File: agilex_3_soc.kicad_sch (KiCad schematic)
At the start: 5 parts, among them J1 Conn_01x14, J2 Conn_02x03_Odd_Even, J3 Conn_02x19_Odd_Even, J4 Conn_01x03, U1 IS43LQ32256A-062BLI

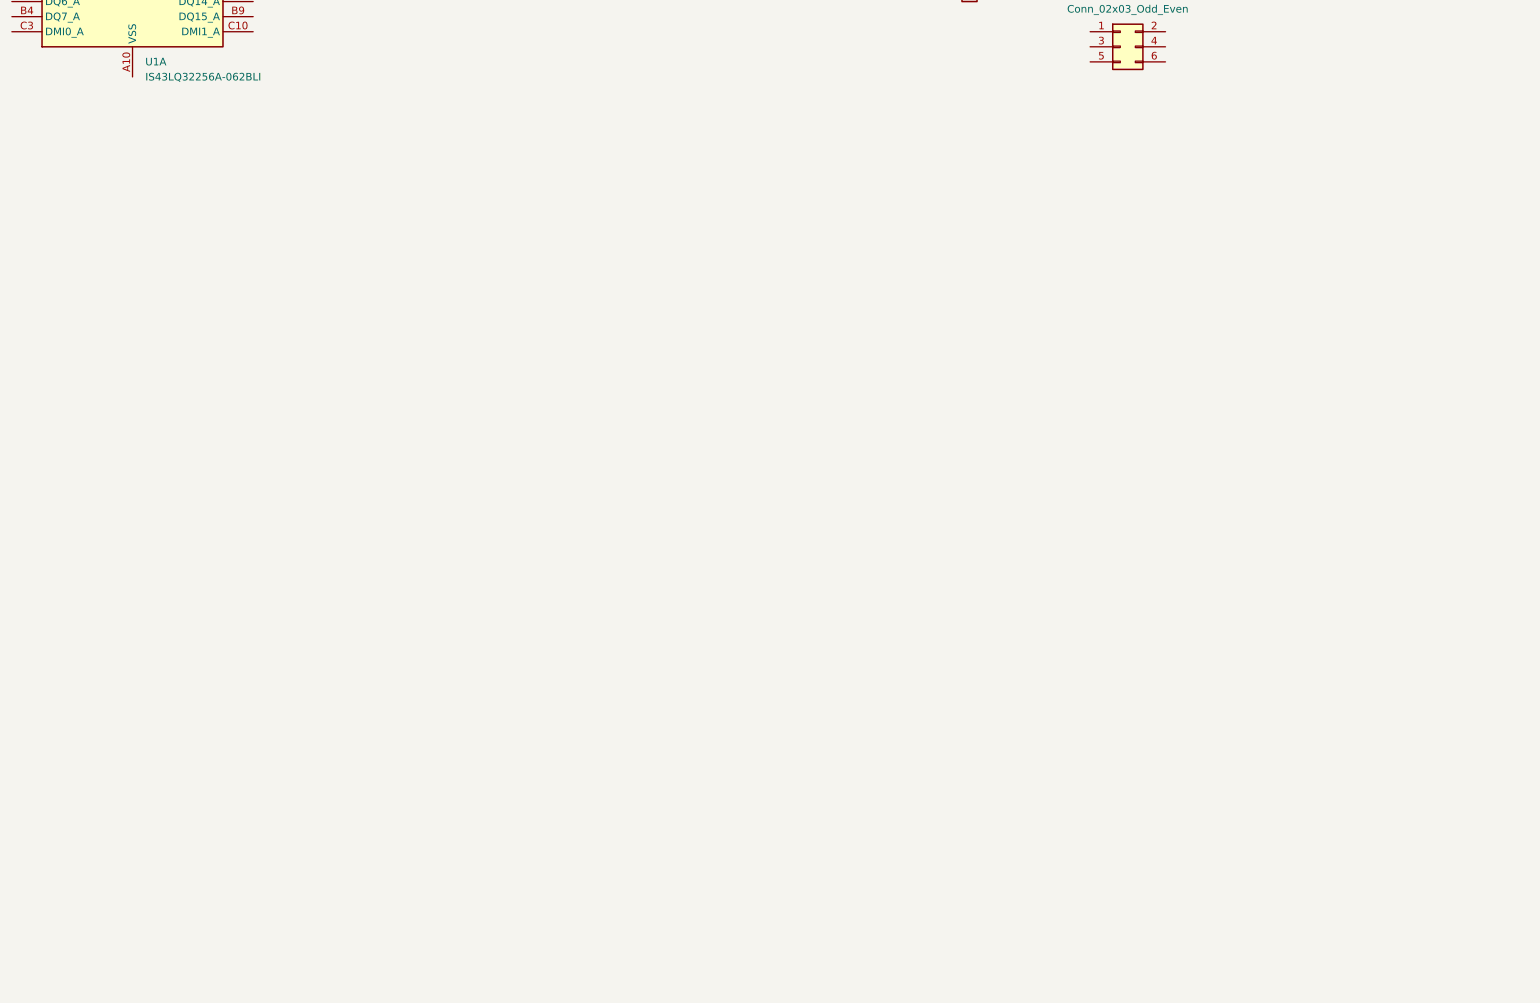
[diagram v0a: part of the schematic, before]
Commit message: sketch out more components from original design
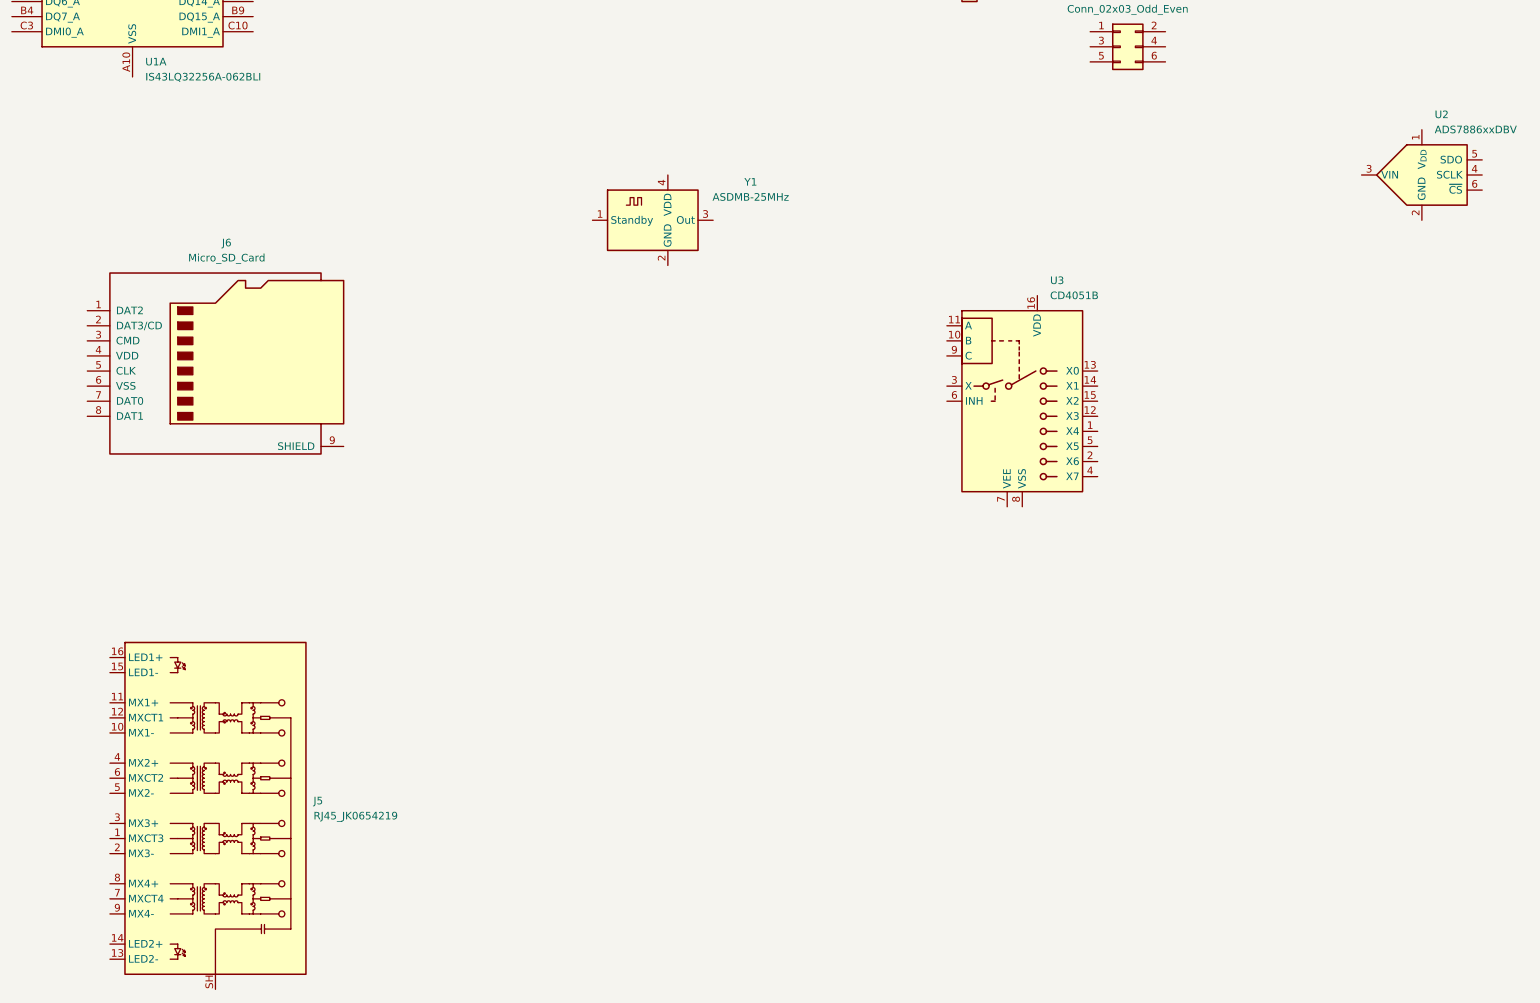
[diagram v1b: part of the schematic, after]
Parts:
- added J5: RJ45_JK0654219, Connector_RJ:RJ45_Pulse_JK0654219NL_Horizontal, symbol Connector:RJ45_JK0654219
- added J6: Micro_SD_Card, Connector_Card:microSD_HC_Hirose_DM3AT-SF-PEJM5, symbol Connector:Micro_SD_Card
- added U2: ADS7886xxDBV, Package_TO_SOT_SMD:SOT-23-6, symbol Analog_ADC:ADS7886xxDBV
- added U3: CD4051B, Package_SO:TSSOP-16_4.4x5mm_P0.65mm, symbol Analog_Switch:CD4051B
- added Y1: ASDMB-25MHz, Oscillator:Oscillator_SMD_Abracon_ASDMB-4Pin_2.5x2.0mm, symbol Oscillator:ASDMB-xxxMHz

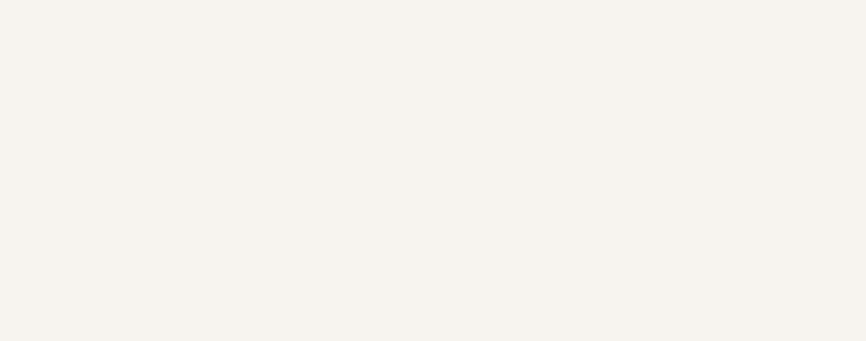
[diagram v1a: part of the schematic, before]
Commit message: add partial libraries
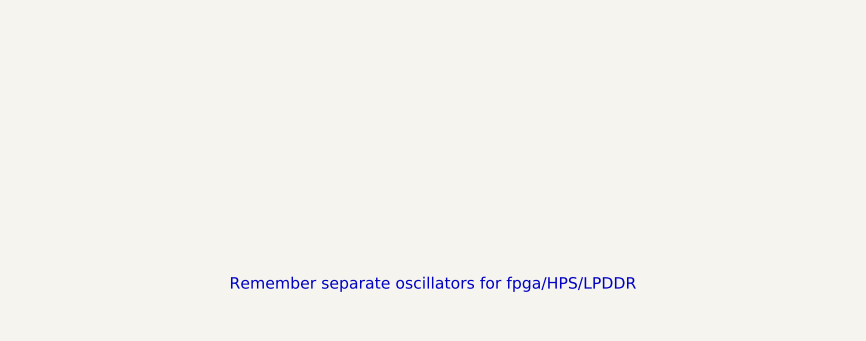
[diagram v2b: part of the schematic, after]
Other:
- note added: "Remember separate oscillators for fpga/HPS/LPDDR"
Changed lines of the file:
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@@
 	(generator_version "9.0")
 	(paper "A3")
+	(text "Remember separate oscillators for fpga/HPS/LPDDR"
+		(exclude_from_sim no)
+		(at 178.308 257.81 0)
+		(effects
+			(font
+				(size 1.27 1.27)
+			)
+		)
+	)
 	(symbol
 		(lib_id "Connector_Generic:Conn_01x03")

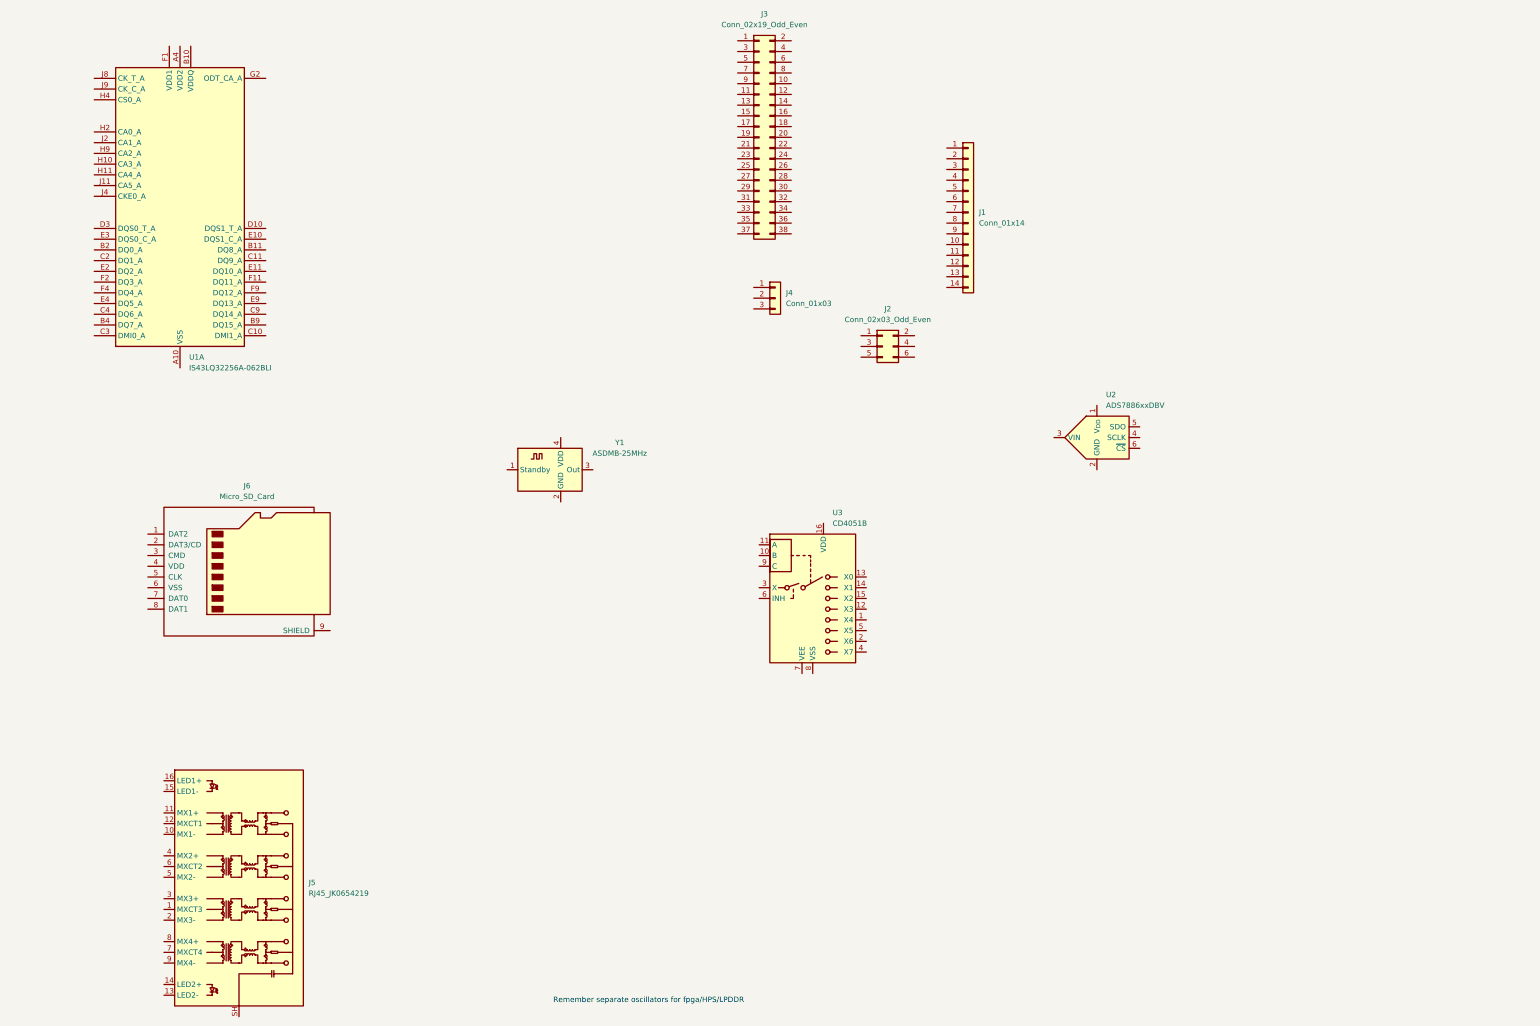
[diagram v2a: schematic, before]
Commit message: start sketching agilex 3 soc schematic and pcb
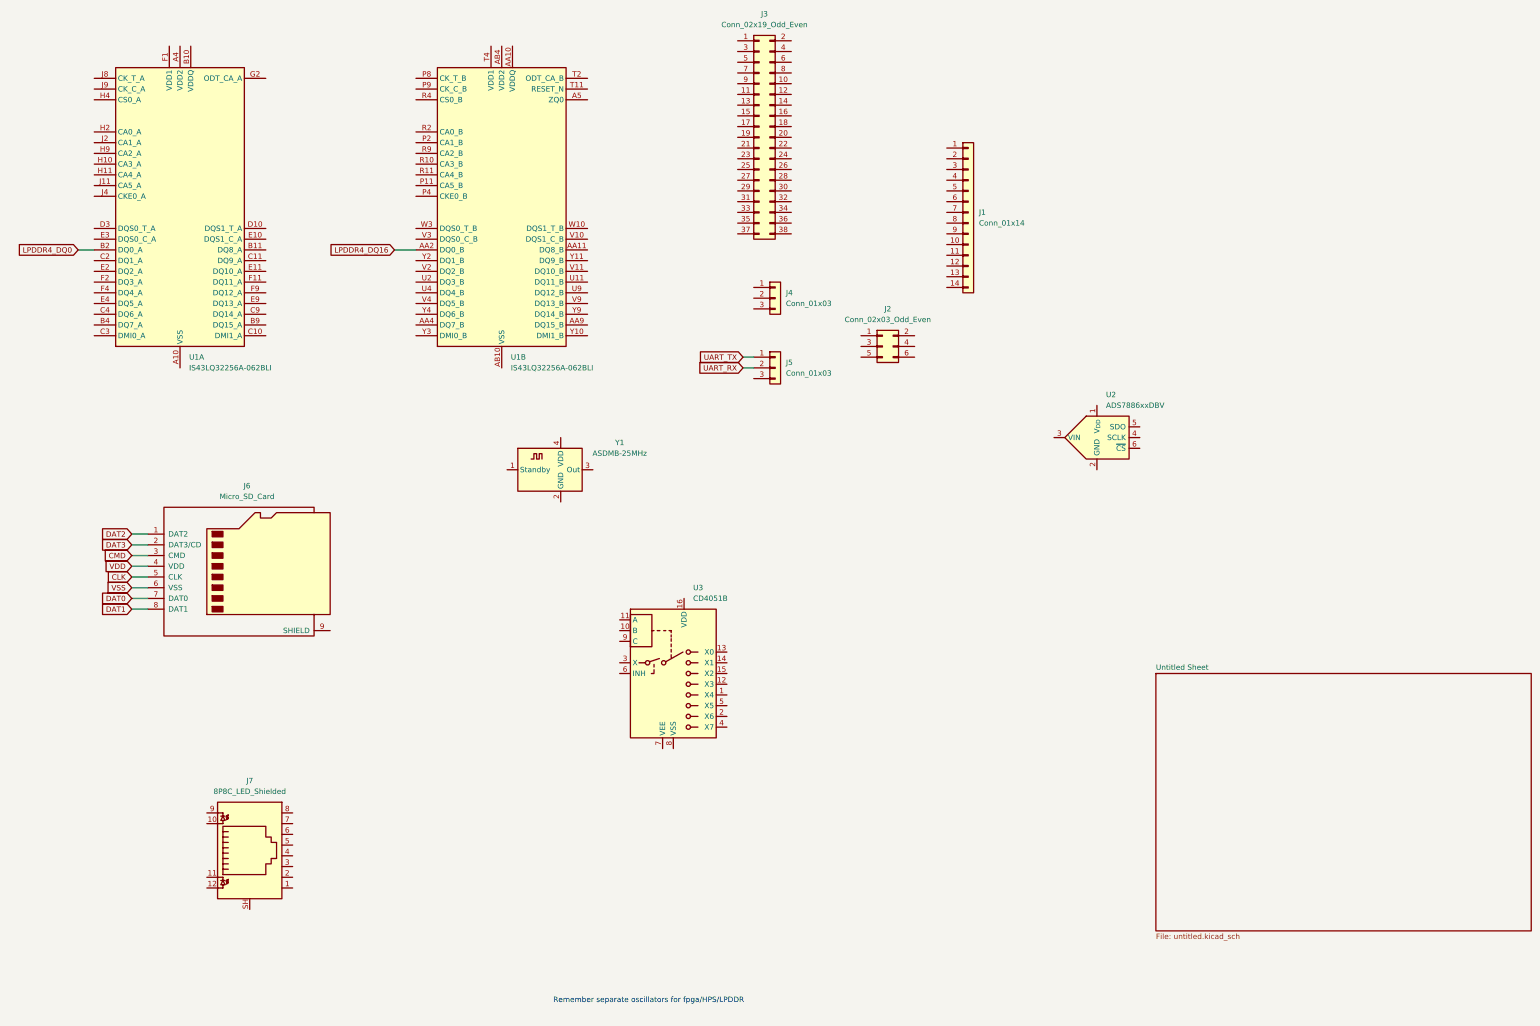
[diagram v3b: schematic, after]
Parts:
- removed J5: RJ45_JK0654219, Connector_RJ:RJ45_Pulse_JK0654219NL_Horizontal, symbol Connector:RJ45_JK0654219
- added J5: Conn_01x03, Connector_PinHeader_2.54mm:PinHeader_1x03_P2.54mm_Vertical, symbol Connector_Generic:Conn_01x03
- added J7: 8P8C_LED_Shielded, Connector_RJ:RJ45_Bel_SI-60062-F, symbol Connector:8P8C_LED_Shielded
- added unit 2 of U1
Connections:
- net DAT2: now reaches J6.1 (DAT2)
- net DAT3: now reaches J6.2 (DAT3/CD)
- net CMD: now reaches J6.3 (CMD)
- net VDD: now reaches J6.4 (VDD)
- net CLK: now reaches J6.5 (CLK)
- net VSS: now reaches J6.6 (VSS)
- net DAT0: now reaches J6.7 (DAT0)
- net DAT1: now reaches J6.8 (DAT1)
- net LPDDR4_DQ0: now reaches U1.B2 (DQ0_A)
- new net: U1.AA10 (VDDQ), U1.AA3 (VDDQ), U1.AA5 (VDDQ), U1.AA8 (VDDQ), U1.U10 (VDDQ), U1.U3 (VDDQ), U1.W1 (VDDQ), U1.W12 (VDDQ), U1.W5 (VDDQ), U1.W8 (VDDQ)
- new net: U1.AB10 (VSS), U1.AB3 (VSS), U1.AB5 (VSS), U1.AB8 (VSS), U1.N11 (VSS), U1.N2 (VSS), U1.N4 (VSS), U1.N9 (VSS), U1.P1 (VSS), U1.P10 (VSS), U1.P12 (VSS), U1.P3 (VSS), U1.T1 (VSS), U1.T10 (VSS), U1.T12 (VSS), U1.T3 (VSS), U1.T5 (VSS), U1.T8 (VSS), U1.V1 (VSS), U1.V12 (VSS), U1.V5 (VSS), U1.V8 (VSS), U1.W11 (VSS), U1.W2 (VSS), U1.W4 (VSS), U1.W9 (VSS), U1.Y1 (VSS), U1.Y12 (VSS), U1.Y5 (VSS), U1.Y8 (VSS)
- new net: U1.AB4 (VDD2), U1.AB9 (VDD2), U1.N1 (VDD2), U1.N10 (VDD2), U1.N12 (VDD2), U1.N3 (VDD2), U1.R1 (VDD2), U1.R12 (VDD2), U1.R5 (VDD2), U1.R8 (VDD2), U1.U5 (VDD2), U1.U8 (VDD2)
- new net: U1.T4 (VDD1), U1.T9 (VDD1), U1.U1 (VDD1), U1.U12 (VDD1)
- new net LPDDR4_DQ16: U1.AA2 (DQ0_B)
- new net UART_RX: J5.2 (Pin_2)
- new net UART_TX: J5.1 (Pin_1)
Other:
- added sheet Untitled Sheet (untitled.kicad_sch)
- moved on the sheet: U3
